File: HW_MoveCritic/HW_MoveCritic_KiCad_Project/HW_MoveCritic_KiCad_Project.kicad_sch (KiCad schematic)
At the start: 43 parts, among them J2 Conn_ARM_SWD_TagConnect_TC2030, J3 USB_C_Receptacle_USB2.0, SW1 SW_Push, U1 STM32WB55CEUx, U2 USBLC6-2P6, U3 MIC5365-3.3YD5, U5 BNO086, X1 32KHz768, X2 32MHz

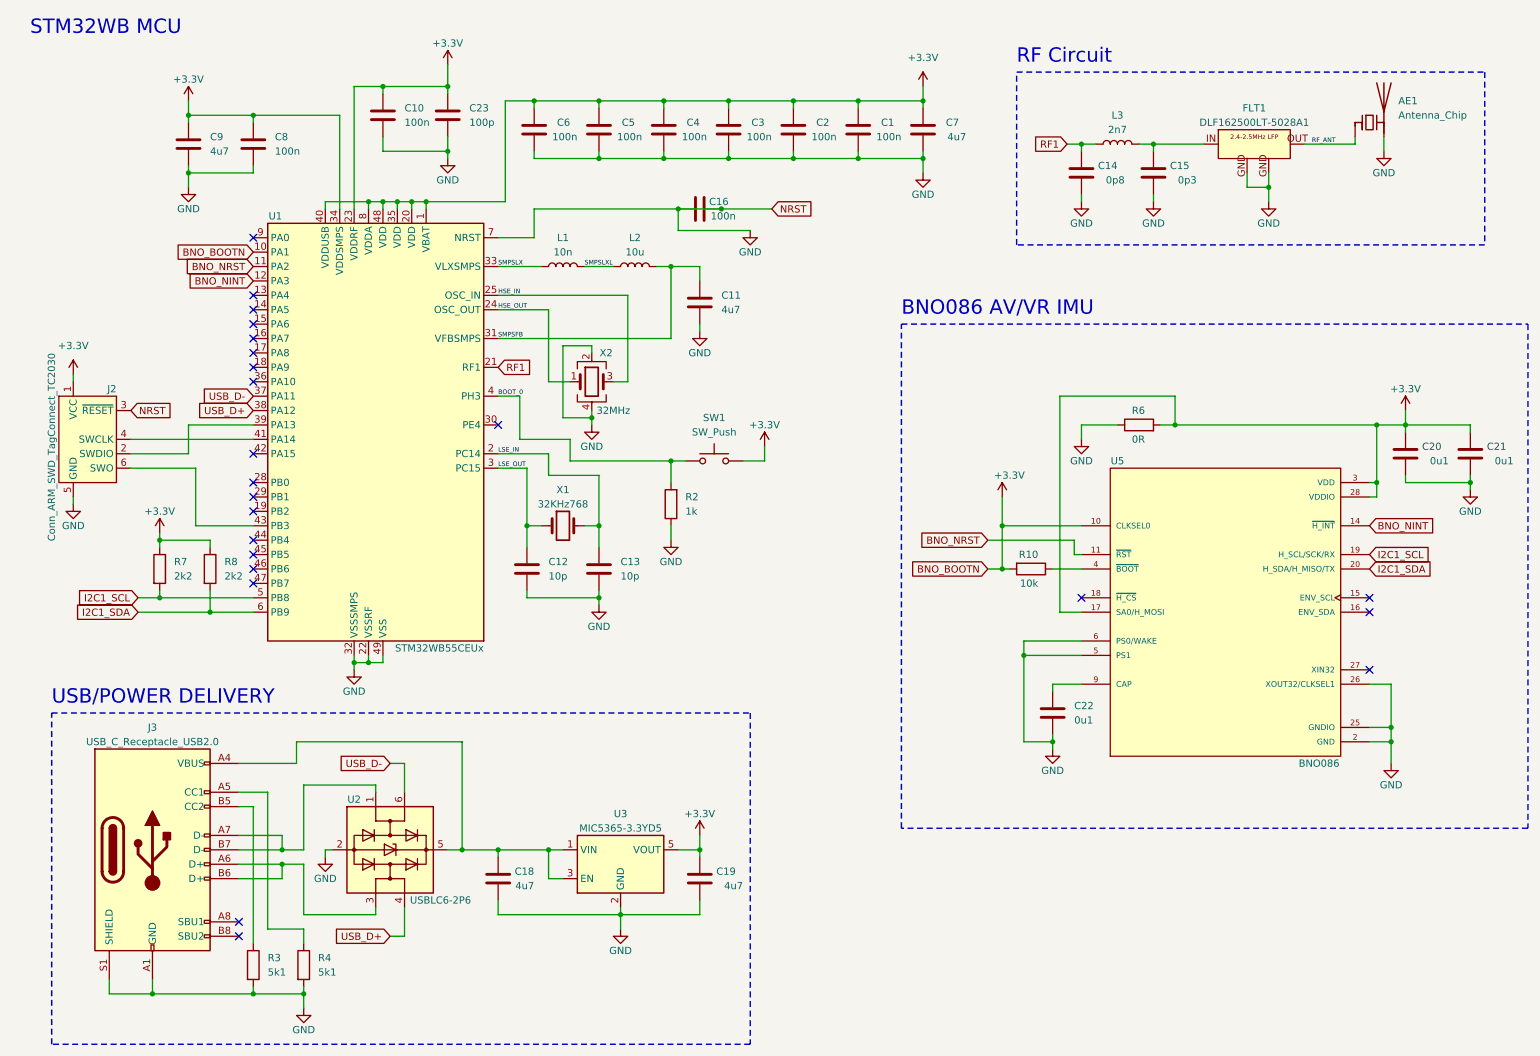
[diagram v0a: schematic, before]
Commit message: V0.1 - Complete Schematic, layout incomplete
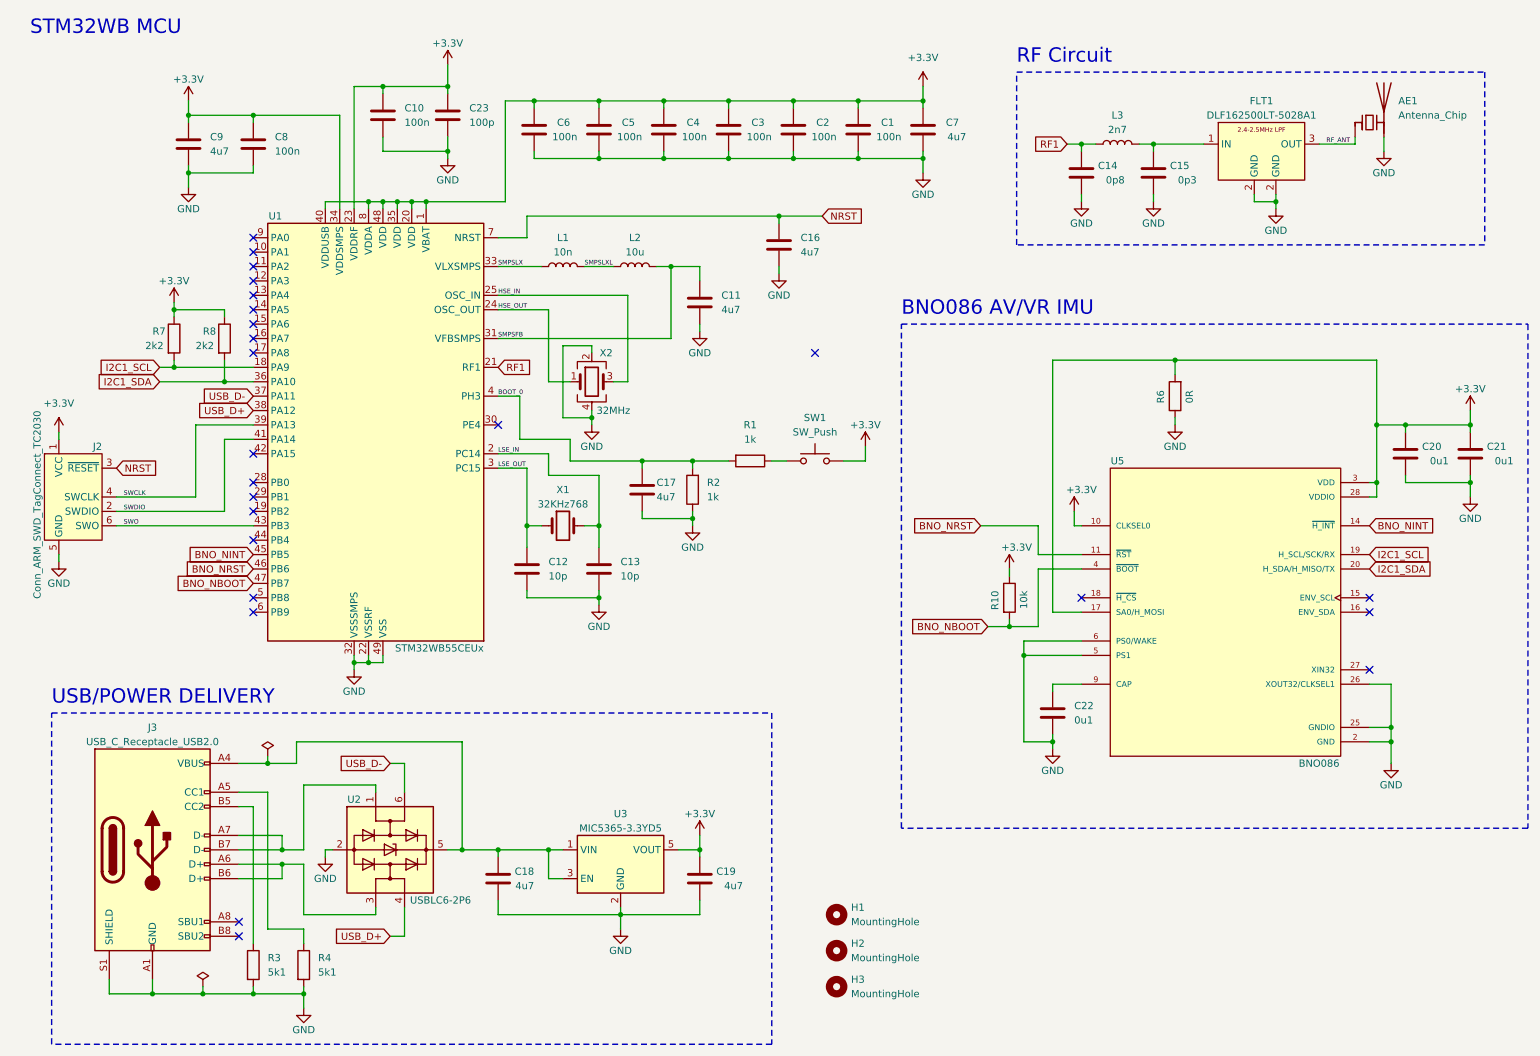
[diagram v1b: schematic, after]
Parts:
- added C17: 4u7, Capacitor_SMD:C_0201_0603Metric, symbol Device:C
- added H1, H2, H3: MountingHole, MountingHole:MountingHole_2.2mm_M2_Pad_Via, symbol Mechanical:MountingHole
- added R1: 1k, Resistor_SMD:R_0603_1608Metric, symbol Device:R
- AE1: footprint (none) -> 830009678:2400MHz_PCB_Meander_Antenna
- C16: value 100n -> 4u7
- SW1: footprint Button_Switch_SMD:SW_Push_1P1T_NO_6x6mm_H9.5mm -> Connector_PinHeader_2.54mm:PinHeader_1x02_P2.54mm_Vertical
- U5: footprint BNO080:IC_BNO080 -> Package_LGA:LGA-28_5.2x3.8mm_P0.5mm
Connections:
- net +3.3V: now also R10.1; no longer R10.2, U1.10 (PA1)
- net BNO_NINT: now also U1.45 (PB5); no longer U1.12 (PA3)
- net BNO_NRST: now also U1.46 (PB6); no longer U1.11 (PA2)
- net BOOT_0: now also C17.1, R1.2; no longer SW1.1
- net GND: now also FLT1.2 (GND), C17.2; no longer C16.1, FLT1.GND, J2.3 (~{RESET}), U1.7 (NRST)
- net I2C1_SCL: now also U1.18 (PA9); no longer U1.5 (PB8)
- net I2C1_SDA: now also U1.36 (PA10); no longer U1.6 (PB9)
- net RF_ANT: now also FLT1.3 (OUT); no longer FLT1.OUT
- net at C15.1, L3.2: now also FLT1.1 (IN); no longer FLT1.IN
- net SWCLK: now reaches U1.39 (PA13)
- net SWCLK: now also J2.4 (SWCLK); no longer J2.2 (SWDIO)
- net SWDIO: now reaches U1.41 (PA14)
- net SWDIO: now also J2.2 (SWDIO); no longer J2.4 (SWCLK)
- net SWO: now reaches J2.6 (SWO), U1.43 (PB3)
- net BNO_NBOOT: now reaches U5.4 (~{BOOT})
- net BNO_NBOOT: now also R10.2, U1.47 (PB7); no longer R10.1
- new net: R1.1, SW1.1
- new net NRST: C16.1, J2.3 (~{RESET}), U1.7 (NRST)
- no-connect marks 23 -> 24
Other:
- company: (none) -> MoveCritic
- title: (none) -> FBT_Module
- moved on the sheet: J2, R10, R2, R6, R7, R8, SW1

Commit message: Large Commit for HW design
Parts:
- removed H3: MountingHole, MountingHole:MountingHole_2.2mm_M2_Pad_Via, symbol Mechanical:MountingHole
- added D2: LED, LED_SMD:LED_0402_1005Metric, symbol Device:LED
- added D?: B5819W, Diode_SMD:D_SOD-123, symbol Device:D_Schottky
- added FID1, FID2, FID3: Fiducial, Fiducial:Fiducial_1mm_Mask2mm, symbol Mechanical:Fiducial
- added H4: MountingHole, MountingHole:MountingHole_2.2mm_M2_DIN965, symbol Mechanical:MountingHole
- added J1: JST_PH_2.00mm, Connector_JST:JST_PH_B2B-PH-K_1x02_P2.00mm_Vertical, symbol Connector:Conn_01x02_Pin
- added R5: 220R, Resistor_SMD:R_0201_0603Metric, symbol Device:R
- AE1: footprint 830009678:2400MHz_PCB_Meander_Antenna -> 830009678:2400MHz_PCB_Inverted_F
- C1, C10, C2, C3, C4, C5, C6, C8: value 100n -> 0u1
- H1, H2: footprint MountingHole:MountingHole_2.2mm_M2_Pad_Via -> MountingHole:MountingHole_2.2mm_M2_DIN965; now left out of the parts list
- U1: value STM32WB55CEUx -> STM32WB55CEU6
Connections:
- net BNO_NBOOT: now also U1.13 (PA4); no longer U1.47 (PB7)
- net BNO_NINT: now also U1.15 (PA6); no longer U1.45 (PB5)
- net BNO_NRST: now also U1.14 (PA5); no longer U1.46 (PB6)
- net GND: now also J1.2 (Pin_2), R5.2
- net +5V: now reaches C18.1, J3.A4 (VBUS), J3.A9 (VBUS), J3.B4 (VBUS), J3.B9 (VBUS), U2.5 (VBUS), U3.1 (VIN), U3.3 (EN)
- net +5V: now also D?.1 (K)
- net at U1.12 (PA3): now also D2.2 (A)
- new net: D2.1 (K), R5.1
- new net VIN: D?.2 (A), J1.1 (Pin_1)
- no-connect marks 24 -> 22
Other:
- moved on the sheet: H1, H2, J2, R7, R8
